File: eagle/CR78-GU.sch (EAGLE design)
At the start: 18 parts, among them Q522 2N3904, Q523 2N3904, Q7 2N3904

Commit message: more schemo
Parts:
- removed Q523: 2N3904, 808_lt:2N3904
- removed R552: 56k, rcl:R-US_0207/5V
- removed R554: 10k, rcl:R-US_0207/10
- added 671, R543: 82k, rcl:R-US_0207/7
- added C4, C5: 68n, rcl:C-US050-025X075
- added D519, D520, D527: (no value), SparkFun-DiscreteSemi:DIODE1N4148
- added Q519, Q520, Q521: 2N3904, 808_lt:2N3904
- added R5, R6: 56k, rcl:R-US_0207/7
- added R546: 2M2, rcl:R-US_0207/7
- added R668: 56k, rcl:R-US_0207/5V
- added R670: 10k, rcl:R-US_0207/10
- added R672: 47k, rcl:R-US_0207/7
- added R673: 5k6, rcl:R-US_0207/7
- added R674: 15k, rcl:R-US_0207/7
- added R675: 10k, rcl:R-US_0207/7
- added R676: 3k9, rcl:R-US_0207/7
- added R677: 18k, rcl:R-US_0207/7
- renumbered Q522 to Q518, R551 to R667, R553 to R669
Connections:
- new net N$1: 671.2, D519.C, R677.2
- new net N$10: R673.1, R674.1, R675.1, R676.2
- new net N$12: R676.1, VR59.E, VR59.S
- new net N$14: R6.1, VR59.A
- new net N$2: C5.1, D519.A, Q520.B, R543.2
- new net N$22: R5.1, R543.1, R6.2, R672.2
- new net N$23: D527.C, R672.1
- new net N$4: Q520.E, Q521.E
- new net N$5: D520.C, Q521.C, R546.2, R675.2
- new net N$6: C5.2, D520.A, R674.2
- new net N$8: C4.2, Q521.B, R5.2
- new net N$9: C4.1, Q520.C, R673.2
- net +12V: now also R670.1; no longer R554.1
- net GND: now also Q519.E, R677.1; no longer Q523.E
- net N$11: now also R668.1; no longer R552.1
- net N$20: now also 671.1
- net N$46: now also D527.A, Q519.C, R670.2; no longer Q523.C, R554.2
- net N$47: now also Q519.B, R668.2; no longer Q523.B, R552.2
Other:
- moved on the sheet: GU-2, GU-4, GU-5, VR59

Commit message: schemo in
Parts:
- added C507: 100/10, rcl:CPOL-USB45181A
- added C531: 22n, rcl:C-US050-025X075
- added C532: 15n, rcl:C-US050-025X075
- added L4: 45mH, rcl:L-US0204/7
- added Q508: 2N3904, 808_lt:2N3904
- added R547: 47k, rcl:R-US_0207/7
- added R548: 470k, rcl:R-US_0207/7
- added R549: 10k, rcl:R-US_0207/7
- added R550: 820, rcl:R-US_0207/7
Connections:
- new net N$13: Q508.B, R547.2, R548.2
- new net N$27: C1.1, C532.2, L4.2, Q508.C
- net +12V: now also C532.1, L4.1, R549.1, R676.1, VR59.E, VR59.S
- net GND: now also C507.-, R550.2
- net N$12: now also C531.1, R546.1, R547.1; no longer R676.1, VR59.E, VR59.S
- net N$26: now also C531.2
- net N$4: now also C507.+, Q508.E, R548.1, R549.2, R550.1
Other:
- moved on the sheet: C1, C2, C3, GU-3, GU-6, JCK1, Q7, R1, R2, R3, R4, R546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

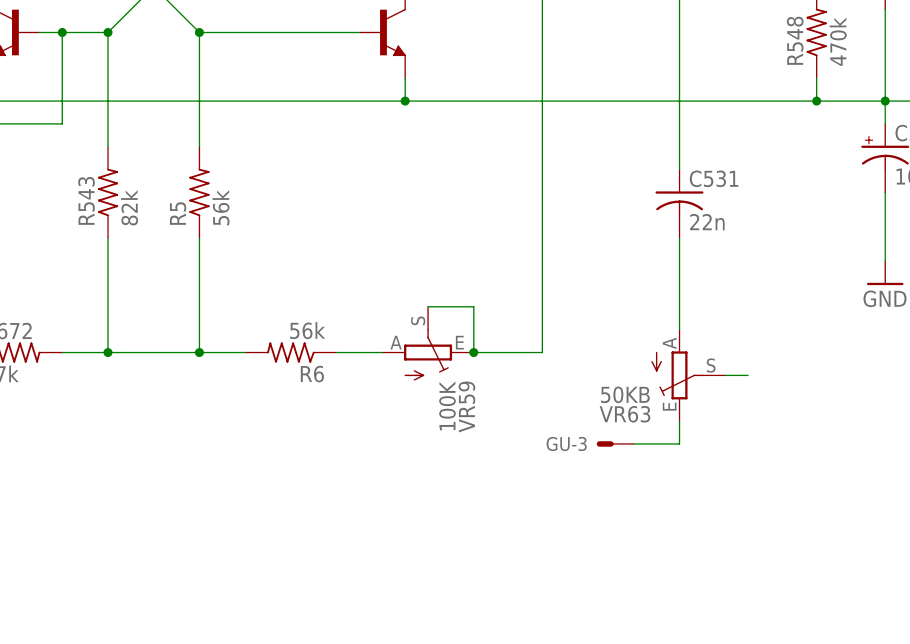
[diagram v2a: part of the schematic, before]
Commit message: fixed noise input and started board
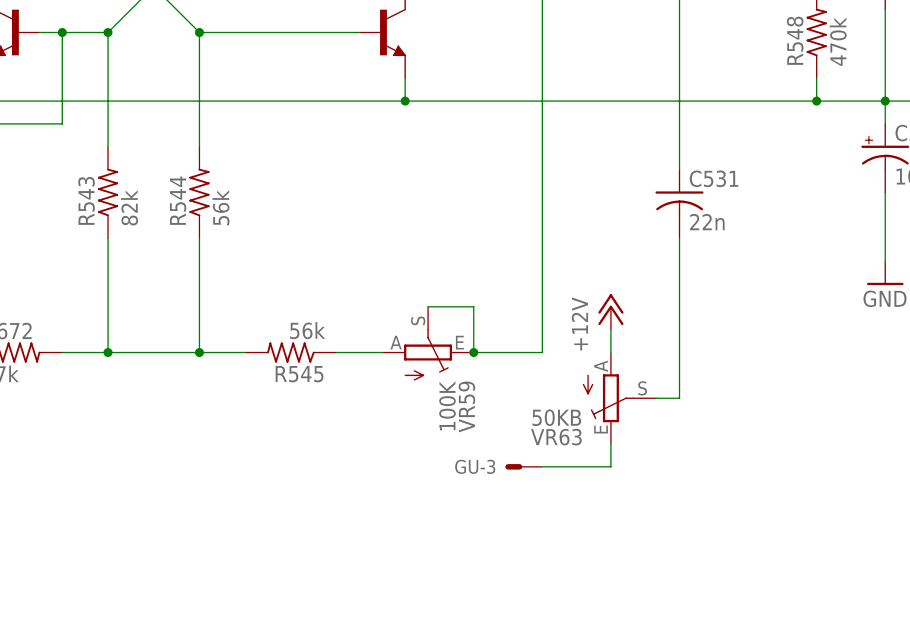
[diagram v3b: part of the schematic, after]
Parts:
- R670: device rcl:R-US_0207/10 -> rcl:R-US_0207/7
- renumbered R5 to R544, R6 to R545
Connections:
- removed net N$26: C531.2, VR63.A
- net +12V: now also VR63.A
- net N$17: now also C531.2
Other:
- moved on the sheet: GU-3, VR63

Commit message: routed with cutout
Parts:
- R667, R668: device rcl:R-US_0207/5V -> rcl:R-US_0207/7
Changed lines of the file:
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@@
 <part name="Q519" library="808_lt" deviceset="2N3904" device=""/>
 <part name="R670" library="rcl" deviceset="R-US_" device="0207/7" value="10k"/>
-<part name="R668" library="rcl" deviceset="R-US_" device="0207/5V" value="56k"/>
+<part name="R668" library="rcl" deviceset="R-US_" device="0207/7" value="56k"/>
 <part name="Q7" library="808_lt" deviceset="2N3904" device=""/>
 <part name="C2" library="rcl" deviceset="C-US" device="050-025X075" value="47p"/>
@@
 <part name="Q518" library="808_lt" deviceset="2N3904" device=""/>
 <part name="R669" library="rcl" deviceset="R-US_" device="0207/7" value="10k"/>
-<part name="R667" library="rcl" deviceset="R-US_" device="0207/5V" value="56k"/>
+<part name="R667" library="rcl" deviceset="R-US_" device="0207/7" value="56k"/>
 <part name="C1" library="rcl" deviceset="C-US" device="050-025X075" value="473"/>
 <part name="VR63" library="TR808clone" deviceset="TRIM_EU-" device="B64Y" value="50KB"/>
